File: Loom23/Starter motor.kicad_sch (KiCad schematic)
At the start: 0 parts

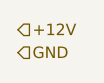
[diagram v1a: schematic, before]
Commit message: Included BSPD and started adding labels
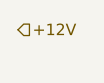
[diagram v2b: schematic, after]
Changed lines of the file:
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@@
 (kicad_sch (version 20211123) (generator eeschema)
   (paper "A4")
-  (hierarchical_label "GND" (shape input) (at 124.46 54.61 0)
-    (effects (font (size 1.27 1.27)) (justify left))
-  )
   (hierarchical_label "+12V" (shape input) (at 124.46 52.07 0)
     (effects (font (size 1.27 1.27)) (justify left))
